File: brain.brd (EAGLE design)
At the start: 100 x 80.3 mm, 28 parts, among them IC1 LP2950ACZ-3.3, IC2 LP2950ACZ-3.3, U1 TINY45-20-DIP, U4 TINY45-20-DIP, U5 TINY45-20-DIP, U6 TINY45-20-DIP

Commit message: pre-autorouter pt. 2
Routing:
- net N$20: track 0.00 -> 26.3 mm
- net N$3: track 0.00 -> 4.60 mm
- net N$19: track 0.00 -> 4.54 mm
- net N$16: track 0.00 -> 3.98 mm

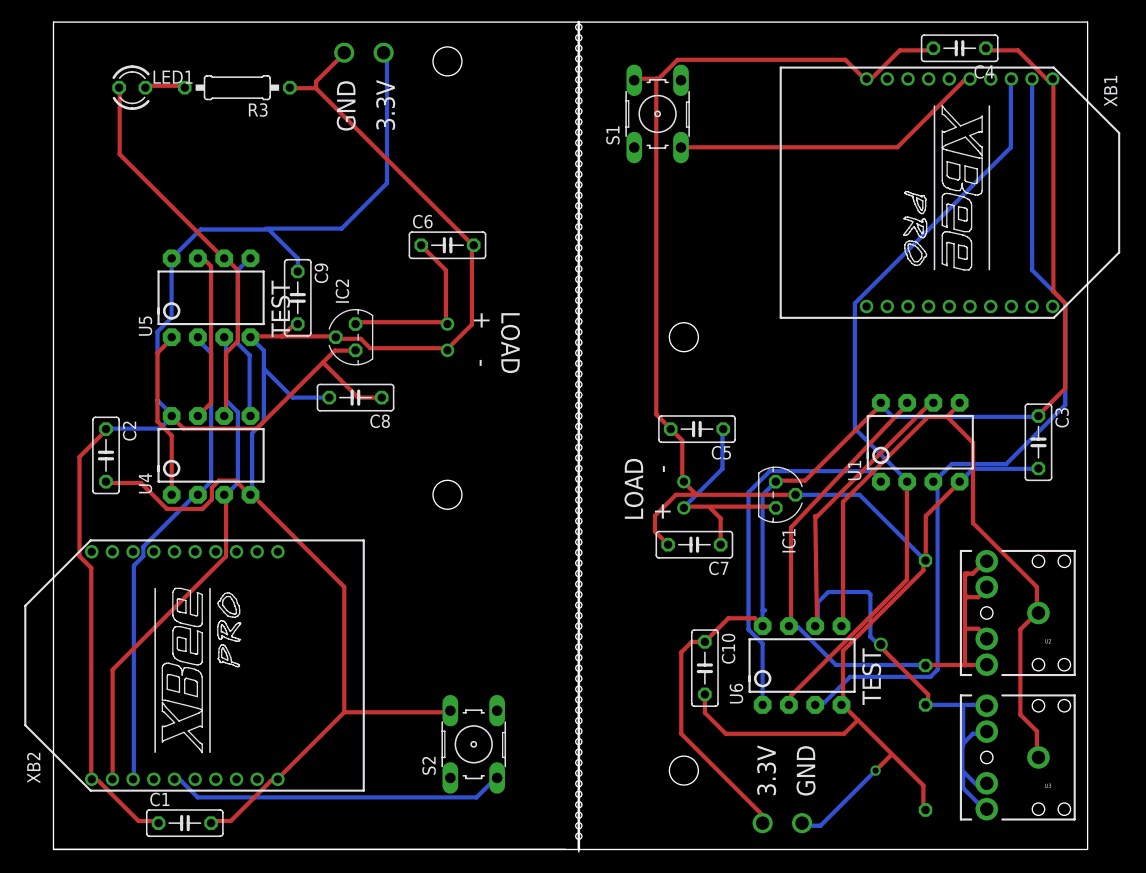
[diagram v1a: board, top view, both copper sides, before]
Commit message: Redid a lot of the routing for wire width and such. pre-changing a few back to smaller wires.
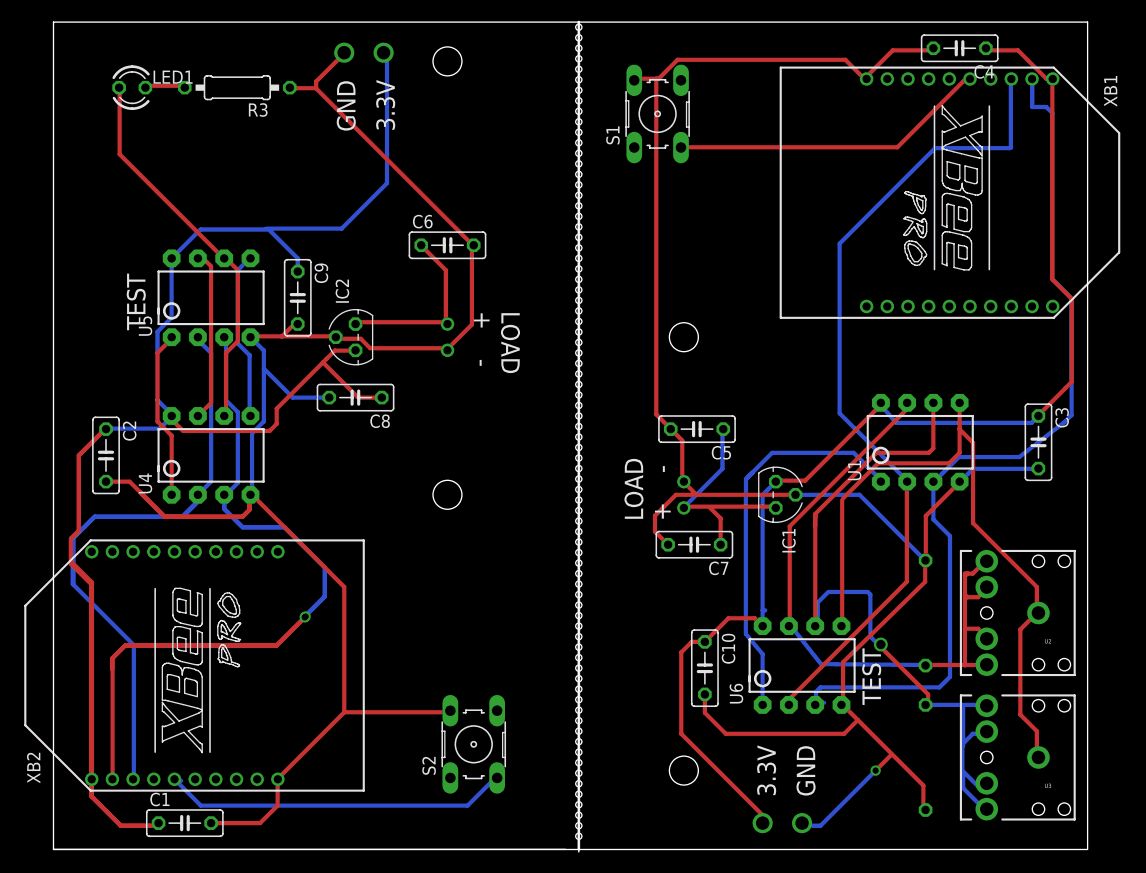
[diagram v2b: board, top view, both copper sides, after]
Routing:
- net RX1: track 80.3 -> 16.6 mm
- net N$26: track 0.00 -> 39.0 mm
- net N$28: track 0.00 -> 35.7 mm
- net N$23: track 0.00 -> 34.1 mm
- net TX1: track 73.6 -> 40.1 mm
- net N$27: track 0.00 -> 30.9 mm
- net VCC1: track 119.3 -> 89.7 mm
- net N$29: track 0.00 -> 28.6 mm
- net PB21: track 46.9 -> 20.9 mm
- net N$22: track 0.00 -> 25.9 mm
- net N$31: track 0.00 -> 21.4 mm, vias 0 -> 1
- net N$21: track 0.00 -> 19.6 mm
- net N$32: track 0.00 -> 19.1 mm
- net RX2: track 48.7 -> 67.5 mm, vias 0 -> 1
- net N$33: track 0.00 -> 18.6 mm
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
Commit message: Fixed all wires. Added the drills for stand offs.
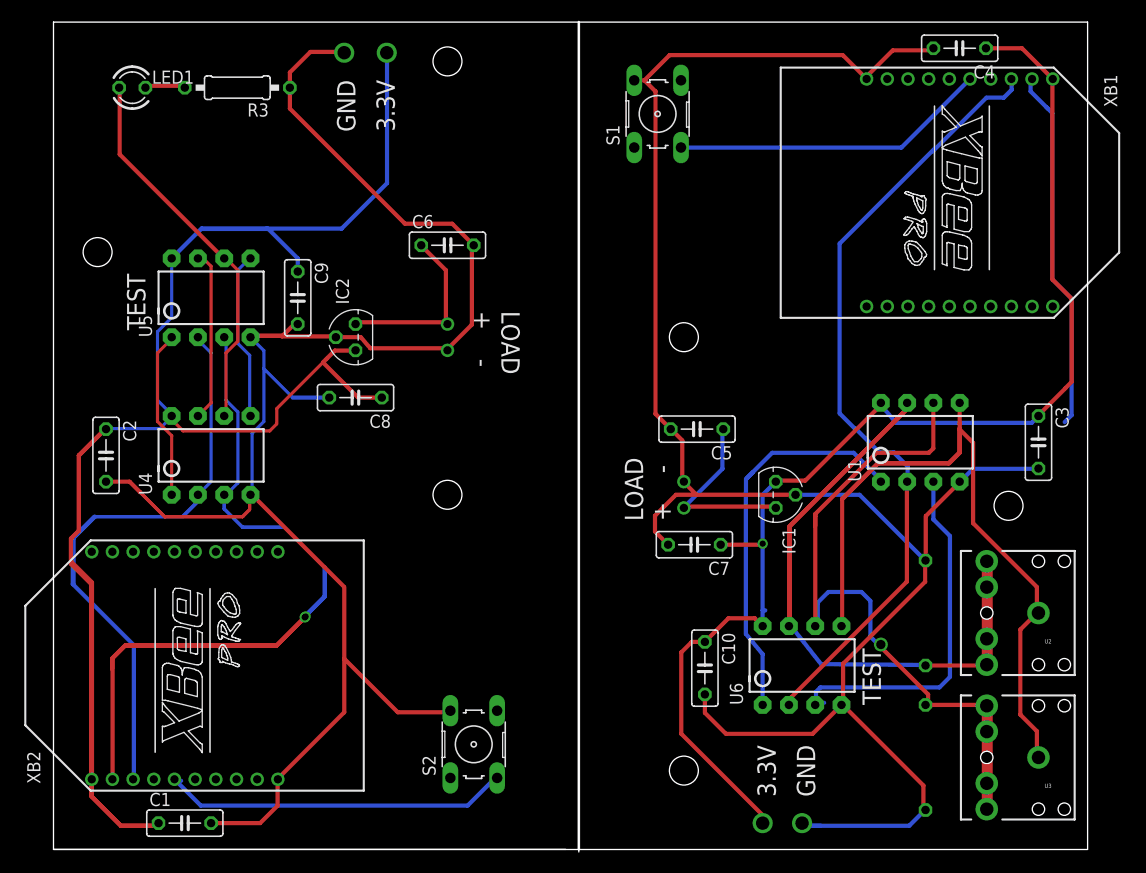
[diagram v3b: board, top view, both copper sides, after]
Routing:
- net PB21: track 20.9 -> 47.2 mm
- net N$9: track 18.0 -> 0.00 mm
- net PB01: track 51.2 -> 66.8 mm
- net RX1: track 16.6 -> 1.50 mm
- net TX1: track 40.1 -> 26.3 mm
- net N$37: track 0.00 -> 11.0 mm
- net GND2: track 151.9 -> 162.7 mm
- net VOUT2: track 114.4 -> 124.7 mm
- net N$2: track 11.0 -> 1.27 mm, vias 1 -> 0
- net PB11: track 17.0 -> 26.5 mm
- net N$10: track 8.42 -> 0.00 mm
- net N$38: track 0.00 -> 8.13 mm
- net N$19: track 4.54 -> 12.2 mm
- net N$26: track 39.0 -> 31.6 mm
- net N$3: track 4.60 -> 0.00 mm
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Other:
- board text added: "Water Management System"
- board text removed: "Well Monitoring System"

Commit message: Most recent board changes. also, added the arduino files for the attiny.
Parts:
- moved U$6 0.68 mm to (40.0, 34.6)
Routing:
- net N$45: track 0.00 -> 38.9 mm
- net N$43: track 0.00 -> 27.7 mm
- net N$42: track 0.00 -> 15.7 mm
- net N$40: track 0.00 -> 9.24 mm
- net N$44: track 0.00 -> 3.96 mm
- net N$41: track 0.00 -> 3.45 mm
- net PB11: track 26.5 -> 27.6 mm
- net VIN2: track 17.5 -> 18.1 mm
- net N$31: vias 1 -> 0
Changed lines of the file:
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@@
 <text x="59.69" y="31.75" size="1.778" layer="21" rot="R90">LOAD
 +    -</text>
-<text x="40.64" y="52.07" size="1.778" layer="21" rot="SR270">LOAD
+<text x="41.0972" y="52.07" size="1.778" layer="21" rot="SR270">LOAD
 +    -</text>
 <text x="80.01" y="13.97" size="1.778" layer="21" rot="R90">TEST</text>
@@
 <text x="31.231890625" y="74.41405" size="1.778" layer="21" rot="R270">3.3V</text>
 <text x="27.421890625" y="74.41405" size="1.778" layer="21" rot="R270">GND</text>
-<rectangle x1="89.7636" y1="17.526" x2="90.8304" y2="28.194" layer="1"/>
-<rectangle x1="89.7636" y1="3.5052" x2="90.8304" y2="14.1732" layer="1"/>
 <hole x="4.2672" y="57.7596" drill="2.8"/>
 <hole x="92.3544" y="33.2232" drill="2.8"/>
 <text x="48.006" y="68.8848" size="2.54" layer="22" rot="MR270">Water Management System</text>
 <text x="97.536" y="65.2272" size="2.54" layer="22" rot="MR270">Water Management System</text>
+<dimension x1="0" y1="0" x2="100" y2="0" x3="50" y3="-2.286" textsize="1.778" layer="16" unit="inch"/>
+<dimension x1="100" y1="-0.01" x2="100" y2="80" x3="109.2708" y3="39.995" textsize="1.778" layer="16" unit="inch"/>
 </plain>
 <attributes>
@@
 <attribute name="OC_FARNELL" value="176432" x="-21.59" y="-36.83" size="1.778" layer="27" rot="R90" display="off"/>
 </element>
-<element name="U$6" library="seniordesign" package="SUNNYBUDDYMOUNT" value="SUNNYBUDDYMOUNT" x="39.37" y="34.29" rot="R180"/>
+<element name="U$6" library="seniordesign" package="SUNNYBUDDYMOUNT" value="SUNNYBUDDYMOUNT" x="39.9796" y="34.5948" rot="R180"/>
 <element name="C1" library="rcl" package="C050-025X075" value="bypass" x="12.7" y="2.54"/>
 <element name="C2" library="rcl" package="C050-025X075" value="bypass" x="5.08" y="38.1" rot="R270"/>
@@
 <wire x1="37.9476" y1="50.9778" x2="29.2608" y2="50.9778" width="0.4064" layer="1"/>
 <wire x1="29.2608" y1="50.9778" x2="29.21" y2="50.8" width="0.4064" layer="1"/>
-<wire x1="37.9476" y1="50.9778" x2="38.1" y2="50.8" width="0.4064" layer="1"/>
+<wire x1="37.9476" y1="50.9778" x2="38.7096" y2="51.1048" width="0.4064" layer="1"/>
 </signal>
 <signal name="N$8">
@@
 <wire x1="38.1762" y1="13.2588" x2="33.2994" y2="13.2588" width="0.4064" layer="1"/>
 <wire x1="33.2994" y1="13.2588" x2="28.1178" y2="18.4404" width="0.4064" layer="1"/>
-<wire x1="38.1762" y1="48.4632" x2="38.1" y2="48.26" width="0" layer="19" extent="1-1"/>
+<wire x1="38.1762" y1="48.4632" x2="38.7096" y2="48.5648" width="0" layer="19" extent="1-1"/>
 <wire x1="37.9476" y1="48.4632" x2="38.1762" y2="48.4632" width="0" layer="19" extent="1-1"/>
 </signal>
@@
 <wire x1="73.681209375" y1="32.28335" x2="85.09" y2="43.18" width="0" layer="19" extent="1-1"/>
 <wire x1="84.328" y1="13.97" x2="73.66848125" y2="21.63234375" width="0" layer="19" extent="1-1"/>
-<wire x1="84.328" y1="13.97" x2="89.9668" y2="13.97" width="0.4064" layer="1"/>
-<wire x1="89.9668" y1="13.97" x2="90.2208" y2="13.716" width="0.4064" layer="1"/>
-<wire x1="90.2208" y1="13.716" x2="90.2208" y2="3.9192" width="0.4064" layer="1"/>
-<wire x1="90.2208" y1="3.9192" x2="90.25" y2="3.89" width="0.4064" layer="1"/>
+<wire x1="84.328" y1="13.97" x2="85.5472" y2="13.97" width="0.4064" layer="1"/>
+<wire x1="85.5472" y1="13.97" x2="87.7824" y2="11.7348" width="0.4064" layer="1"/>
+<wire x1="87.7824" y1="11.7348" x2="87.7824" y2="9.6012" width="0.4064" layer="1"/>
+<wire x1="87.7824" y1="8.8392" x2="87.7824" y2="6.3576" width="0.4064" layer="1"/>
+<wire x1="87.7824" y1="6.3576" x2="90.25" y2="3.89" width="0.4064" layer="1"/>
+<wire x1="87.7824" y1="9.6012" x2="87.7824" y2="8.8392" width="0.4064" layer="1"/>
+<wire x1="87.7824" y1="8.8392" x2="90.3732" y2="6.2484" width="0.4064" layer="1"/>
 </signal>
 <signal name="PB51">
@@
 <wire x1="6.941971875" y1="19.725359375" x2="21.587840625" y2="19.725359375" width="0.4064" layer="1"/>
 <wire x1="21.587840625" y1="19.725359375" x2="24.3815625" y2="22.51908125" width="0.4064" layer="1"/>
-<via x="24.3815625" y="22.51908125" extent="1-16" drill="0.6" shape="square"/>
 </signal>
 <signal name="N$32">
@@
 <wire x1="94.488" y1="73.3044" x2="96.1644" y2="71.628" width="0.4064" layer="16"/>
 </signal>
+<signal name="N$40">
+<wire x1="84.4296" y1="13.8684" x2="86.868" y2="13.8684" width="0.4064" layer="1"/>
+<wire x1="87.7824" y1="13.8684" x2="90.2208" y2="13.8684" width="0.4064" layer="1"/>
+<wire x1="86.868" y1="13.8684" x2="87.7824" y2="13.8684" width="0.4064" layer="1"/>
+<wire x1="87.7824" y1="13.8684" x2="90.2208" y2="11.43" width="0.4064" layer="1"/>
+</signal>
+<signal name="N$41">
+<wire x1="87.7824" y1="17.8308" x2="90.2208" y2="20.2692" width="0.4064" layer="1"/>
+</signal>
+<signal name="N$42">
+<wire x1="84.582" y1="17.6784" x2="84.7344" y2="17.6784" width="0.4064" layer="1"/>
+<wire x1="84.7344" y1="17.6784" x2="87.9348" y2="20.8788" width="0.4064" layer="1"/>
+<wire x1="87.9348" y1="20.8788" x2="87.9348" y2="22.098" width="0.4064" layer="1"/>
+<wire x1="87.9348" y1="23.0124" x2="87.9348" y2="25.6032" width="0.4064" layer="1"/>
+<wire x1="87.9348" y1="25.6032" x2="90.0684" y2="27.7368" width="0.4064" layer="1"/>
+<wire x1="87.9348" y1="22.098" x2="87.9348" y2="23.0124" width="0.4064" layer="1"/>
+<wire x1="87.9348" y1="23.0124" x2="90.2208" y2="25.2984" width="0.4064" layer="1"/>
+</signal>
+<signal name="N$43">
+<wire x1="38.862" y1="48.3108" x2="51.6636" y2="35.5092" width="0.4064" layer="1"/>
+<wire x1="51.6636" y1="35.5092" x2="61.2648" y2="35.5092" width="0.4064" layer="1"/>
+</signal>
+<signal name="N$44">
+<wire x1="56.8452" y1="33.0708" x2="60.8076" y2="33.0708" width="0.4064" layer="16"/>
+</signal>
+<signal name="N$45">
+<wire x1="26.5176" y1="43.7388" x2="40.8432" y2="29.4132" width="0.4064" layer="16"/>
+<wire x1="40.8432" y1="29.4132" x2="59.436" y2="29.4132" width="0.4064" layer="16"/>
+</signal>
 </signals>
